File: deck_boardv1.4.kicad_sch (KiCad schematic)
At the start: 47 parts, among them J1 430450800, Q4 MMBT3904, Q6 2N7002, SW1 Inhibit Switch (SS-5GL?), SW3 Inhibit Switch (SS-5GL?), U1 Raspberry Pi Zero 2 W, U2 LT8610AC, U3 DIGI XBee-PRO 900HP RF Module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, U4 ADP7159ACPZ-04-R7

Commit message: adjustments have been made, PCB is also done
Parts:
- removed R13: 178kΩ, Resistor_SMD:R_0201_0603Metric, symbol Device:R_US
- removed U4: ADP7159ACPZ-04-R7, ADP7159ACPZ-04-R7:SON50P300X300X80-11N, symbol ADP7159ACPZ-04-R7:ADP7159ACPZ-04-R7
- added J4, J5, J6, J7: Conn_01x01_Pin, Connector_Wire:SolderWire-0.75sqmm_1x01_D1.25mm_OD2.3mm, symbol Connector:Conn_01x01_Pin
- added R11: 10kΩ, Resistor_SMD:R_0201_0603Metric, symbol Device:R_US
- added U4: ADP7158ARDZ-3.3-R7, ADP7158ARDZ-3.3-R7:SOIC127P600X175-9N, symbol ADP7158ARDZ-3.3-R7:ADP7158ARDZ-3.3-R7
- D1: renamed from D2; footprint STPS5H100B:DPAK -> Schottky:DPAK
- D3: renamed from D1; footprint STPS5H100B:DPAK -> Schottky:DPAK
- R12: value 102kΩ -> 100kΩ
- R3: renamed from R16; value 191kΩ -> 187kΩ
- SW1: value Inhibit Switch (SS-5GL?) -> Inhibit Switch (SS-5GL); footprint (none) -> SS-5GL111:SS-5GL111
- SW2: renamed from SW3; value Inhibit Switch (SS-5GL?) -> Inhibit Switch (SS-5GL); footprint (none) -> SS-5GL111:SS-5GL111
- renumbered C18 to C1, C8 to C13, C15 to C14, C16 to C15, C19 to C16, C1 to C18, C20 to C19, C14 to C8, D4 to D2, D6 to D4, D8 to D5, L3 to L1, Q4 to Q1, Q6 to Q2, R18 to R1, R4 to R10, R1 to R13, R15 to R2, R17 to R4, R19 to R5, R14 to R6, R20 to R7, R27 to R8, R3 to R9
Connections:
- net 28v_IN is gone; now on net 28V: D1.3
- net 28V_POST-INHIB: now also C18.1, R13.2, SW1.1 (A), J5.1 (Pin_1)
- net 3V3: now also U4.1 (VOUT), U4.2 (VOUT_SENSE)
- net 5V_Pi: now also U4.4 (EN), U4.8 (VIN)
- net ENABLE: now also SW2.1 (A), J7.1 (Pin_1); no longer SW2.3 (C)
- net GND: now also R11.2, U4.9 (EPAD); no longer R12.1
- net TE_2: now also R12.1
- net at C10.2: now also U4.7 (VREG)
- net at R12.2: now also U1.15 (GPIO22-TE-2), R11.1
- net at C11.2: now also U4.3 (BYP)
- net at C9.1: now also U4.5 (REF_SENSE), U4.6 (REF)
- net at D3.2, SW2.2 (B): now also J6.1 (Pin_1)
- net at D1.2, SW1.2 (B): now also J4.1 (Pin_1)
- removed net 28V_Post_Inhibit: C18.1, R13.2, SW1.3 (C)
- no-connect marks 49 -> 48
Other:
- moved on the sheet: C10, C11, C12, C13, C17, C18, C19, C9, D1, D2, D3, R10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

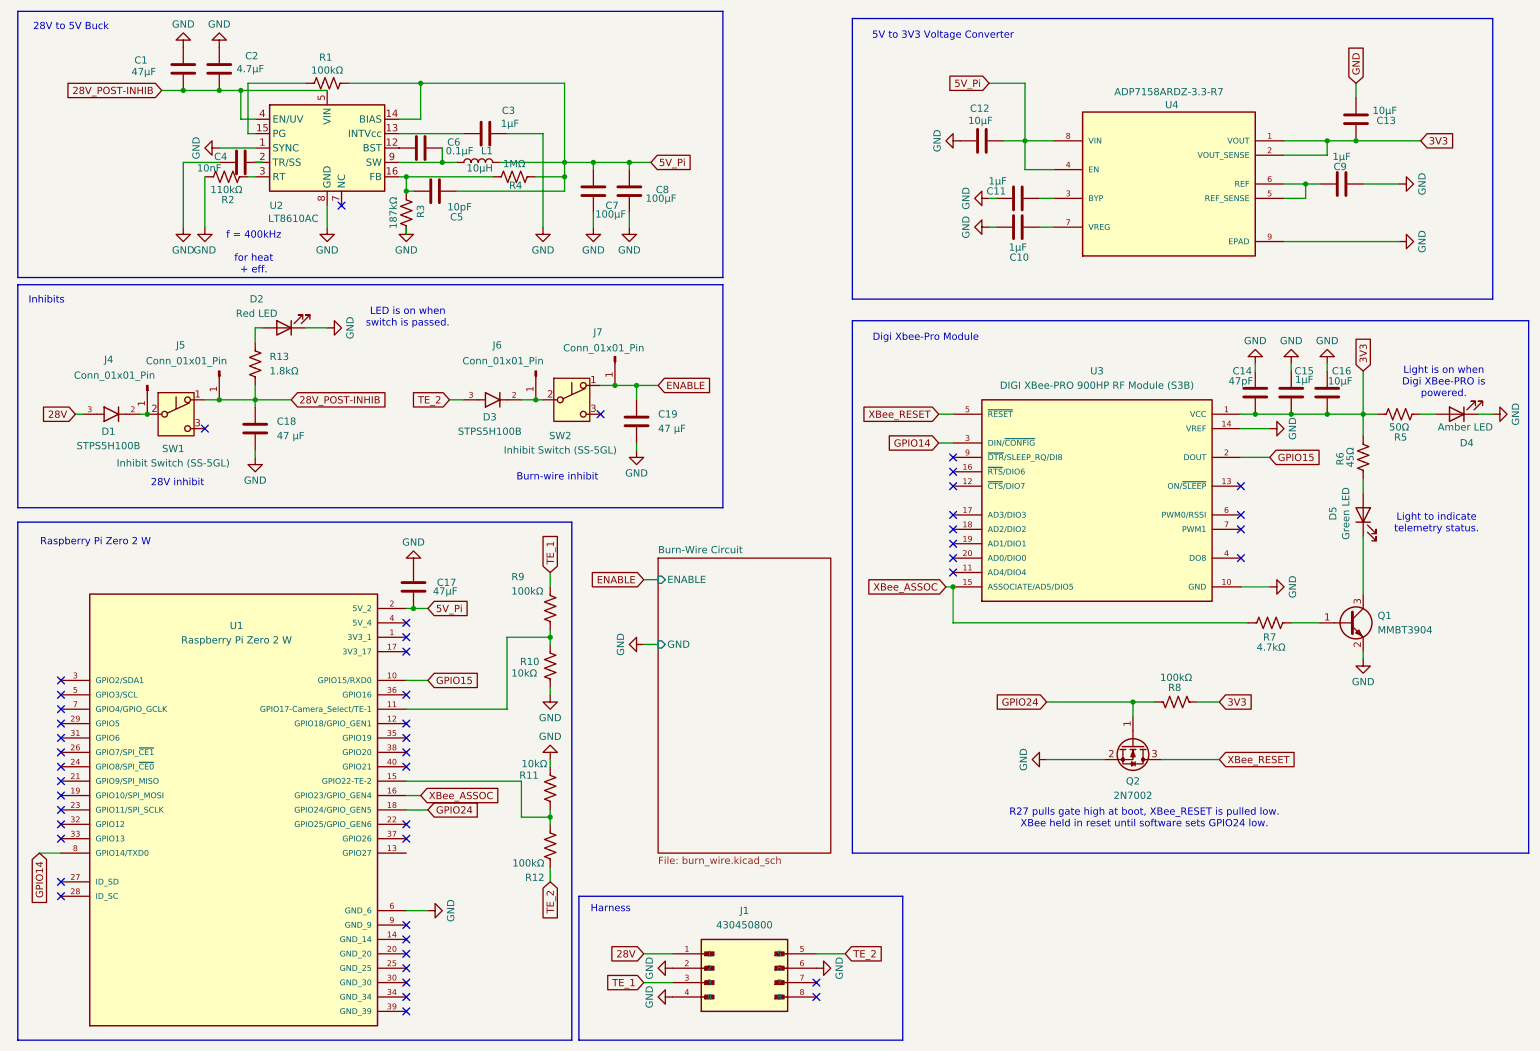
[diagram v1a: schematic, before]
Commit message: Resolved errors and warnings.
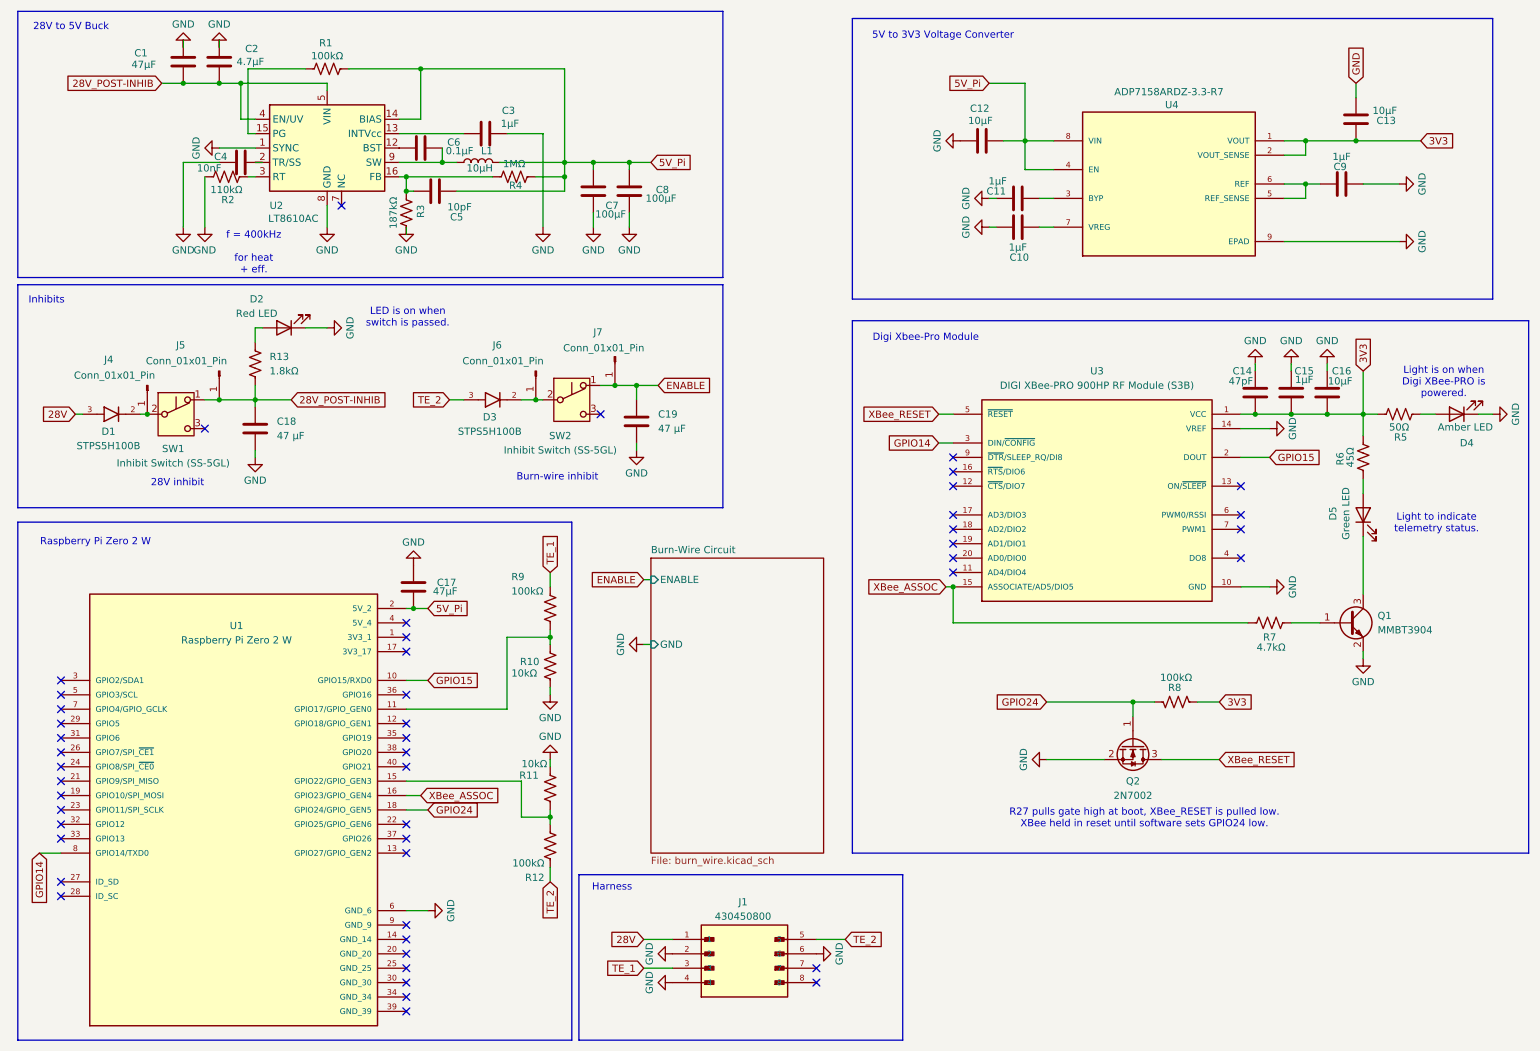
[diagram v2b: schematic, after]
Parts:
- U1: footprint Raspberry Pi Zero 2 W:MODULE_SC1176 -> SC1176:MODULE_SC1176
- U4: footprint ADP7158ARDZ-3.3-R7:SOIC127P600X175-9N -> ADP7158ARDZ-3.3-R7-2:SOIC127P600X175-9N
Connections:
- no-connect marks 48 -> 49
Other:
- moved on the sheet: C1, C2, J1, R1

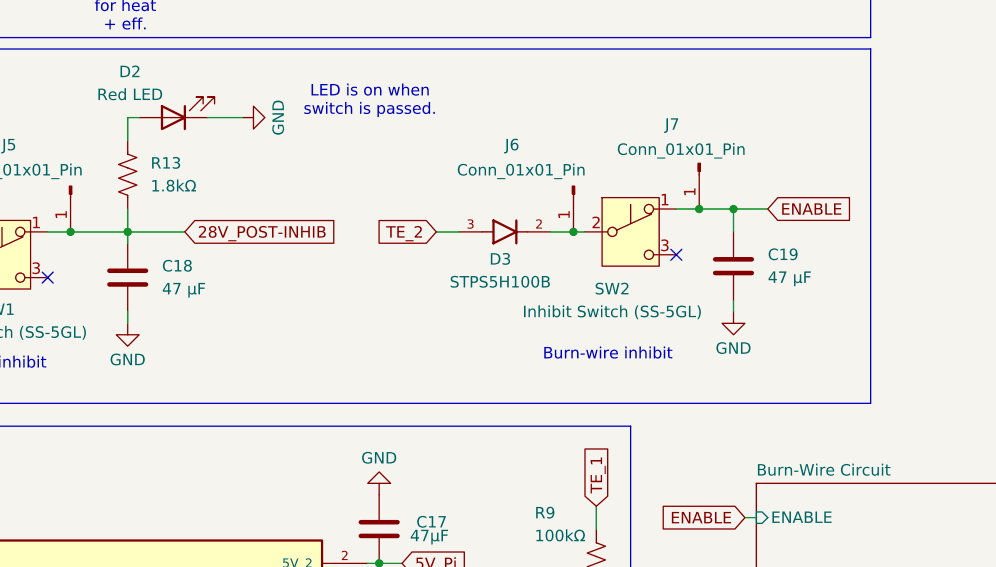
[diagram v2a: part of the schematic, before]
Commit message: Resolved manufacturer design rules
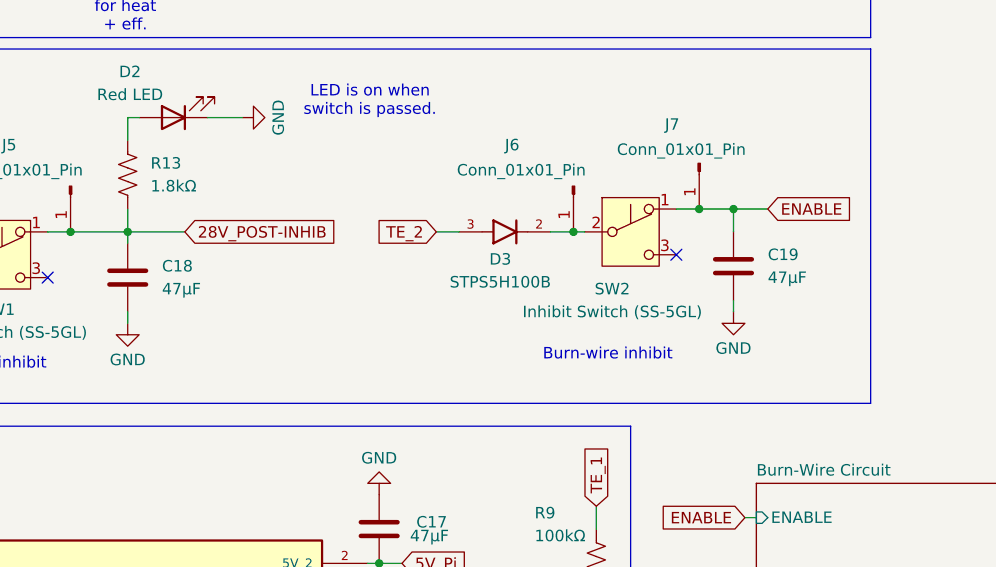
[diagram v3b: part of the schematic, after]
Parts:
- C18, C19: value 47 µF -> 47µF
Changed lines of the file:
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@@
 			)
 		)
-		(property "Value" "47 µF"
+		(property "Value" "47µF"
 			(at 63.5 88.8999 0)
 			(effects
@@
 			)
 		)
-		(property "Value" "47 µF"
+		(property "Value" "47µF"
 			(at 130.81 87.6299 0)
 			(effects
